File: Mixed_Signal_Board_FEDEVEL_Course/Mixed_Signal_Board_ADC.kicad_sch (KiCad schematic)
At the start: 12 parts, among them U1 REF3033AIDBZT, U300 ADC141S626CIMM_NOPB

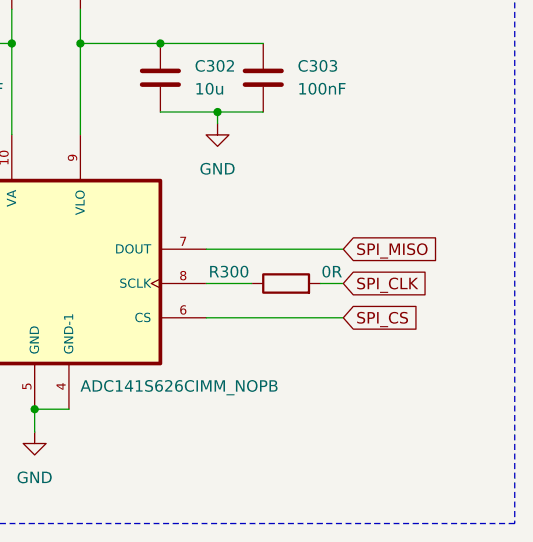
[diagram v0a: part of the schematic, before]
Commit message: Add ADC sch
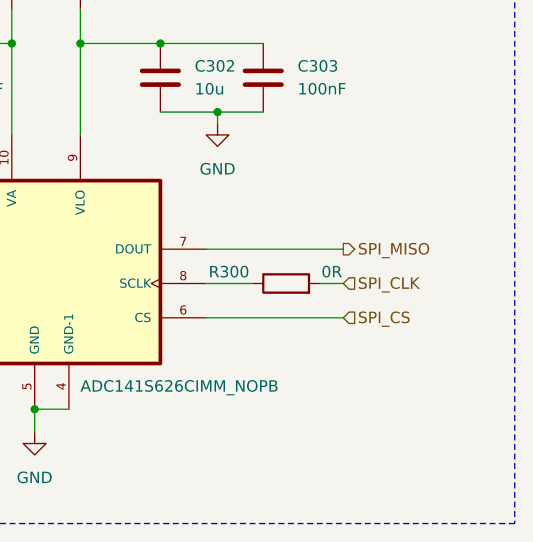
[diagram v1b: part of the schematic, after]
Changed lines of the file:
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@@
 		)
 	)
-	(global_label "SPI_MISO"
+	(hierarchical_label "SPI_CS"
 		(shape input)
-		(at 182.88 69.85 0)
-		(fields_autoplaced yes)
+		(at 182.88 77.47 0)
 		(effects
 			(font
@@
 			(justify left)
 		)
-		(property "Intersheetrefs" "${INTERSHEET_REFS}"
-			(at 194.5133 69.85 0)
-			(hide yes)
-			(show_name no)
-			(do_not_autoplace no)
-			(effects
-				(font
-					(size 1.27 1.27)
-				)
-				(justify left)
-			)
-		)
 	)
-	(global_label "SPI_CLK"
+	(hierarchical_label "SPI_CLK"
 		(shape input)
 		(at 182.88 73.66 0)
-		(fields_autoplaced yes)
 		(effects
 			(font
@@
 			(justify left)
 		)
-		(property "Intersheetrefs" "${INTERSHEET_REFS}"
-			(at 193.4852 73.66 0)
-			(hide yes)
-			(show_name no)
-			(do_not_autoplace no)
-			(effects
-				(font
-					(size 1.27 1.27)
-				)
-				(justify left)
-			)
-		)
 	)
-	(global_label "SPI_CS"
-		(shape input)
-		(at 182.88 77.47 0)
-		(fields_autoplaced yes)
+	(hierarchical_label "SPI_MISO"
+		(shape output)
+		(at 182.88 69.85 0)
 		(effects
 			(font
@@
 			(justify left)
 		)
-		(property "Intersheetrefs" "${INTERSHEET_REFS}"
-			(at 192.3966 77.47 0)
-			(hide yes)
-			(show_name no)
-			(do_not_autoplace no)
-			(effects
-				(font
-					(size 1.27 1.27)
-				)
-				(justify left)
-			)
-		)
 	)

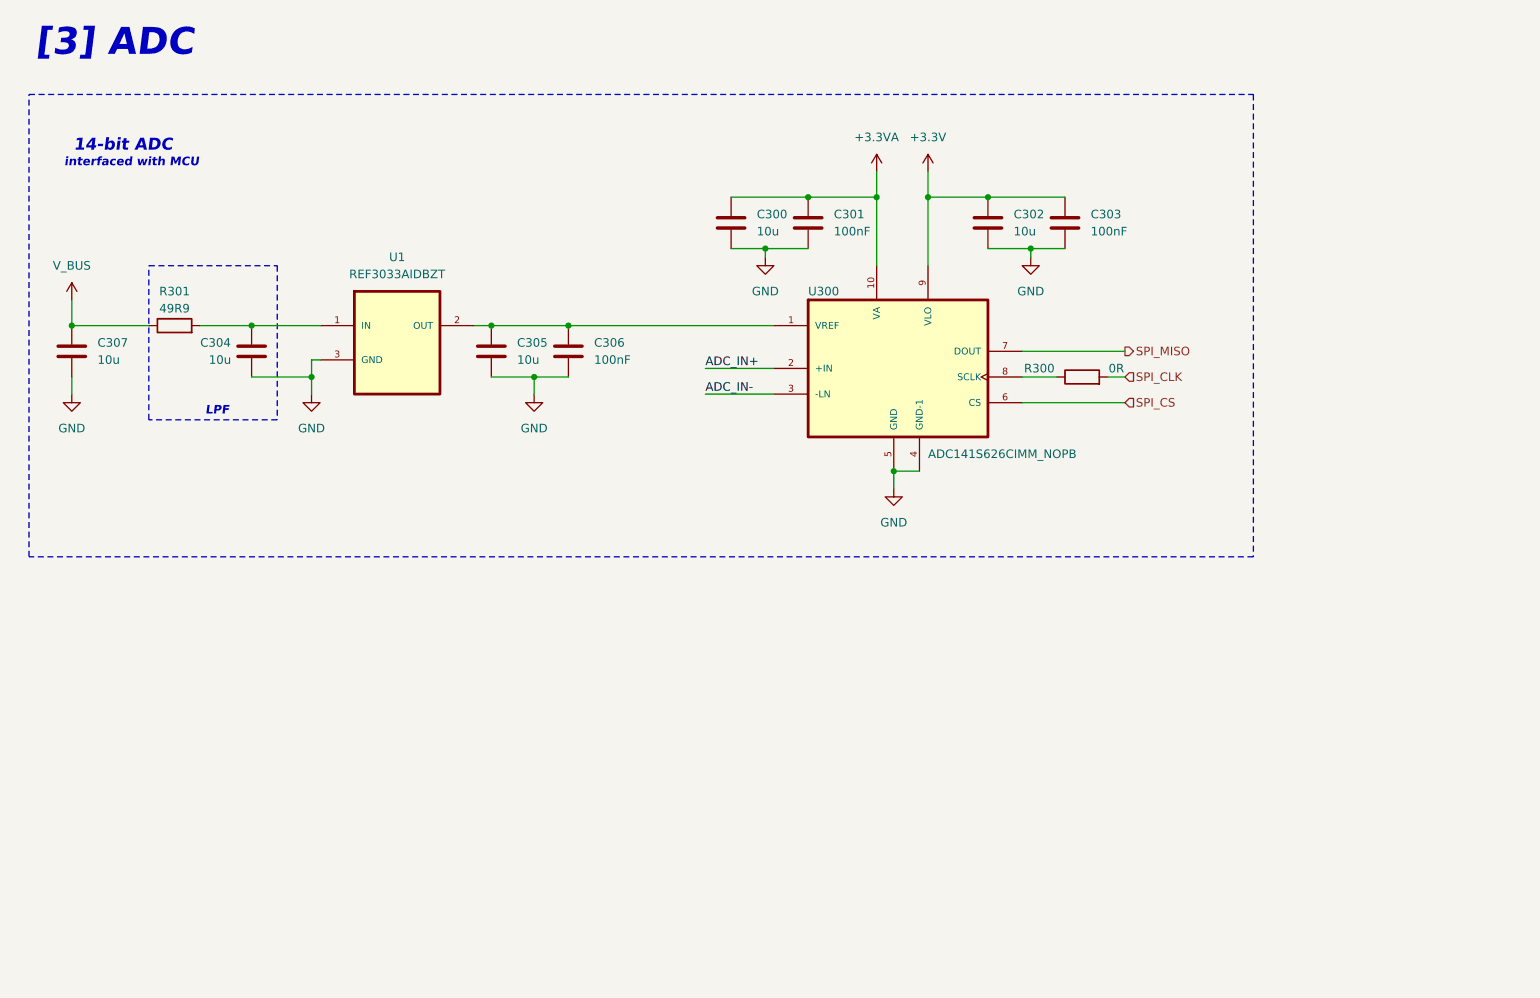
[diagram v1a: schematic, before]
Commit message: Complete the sch of ADC
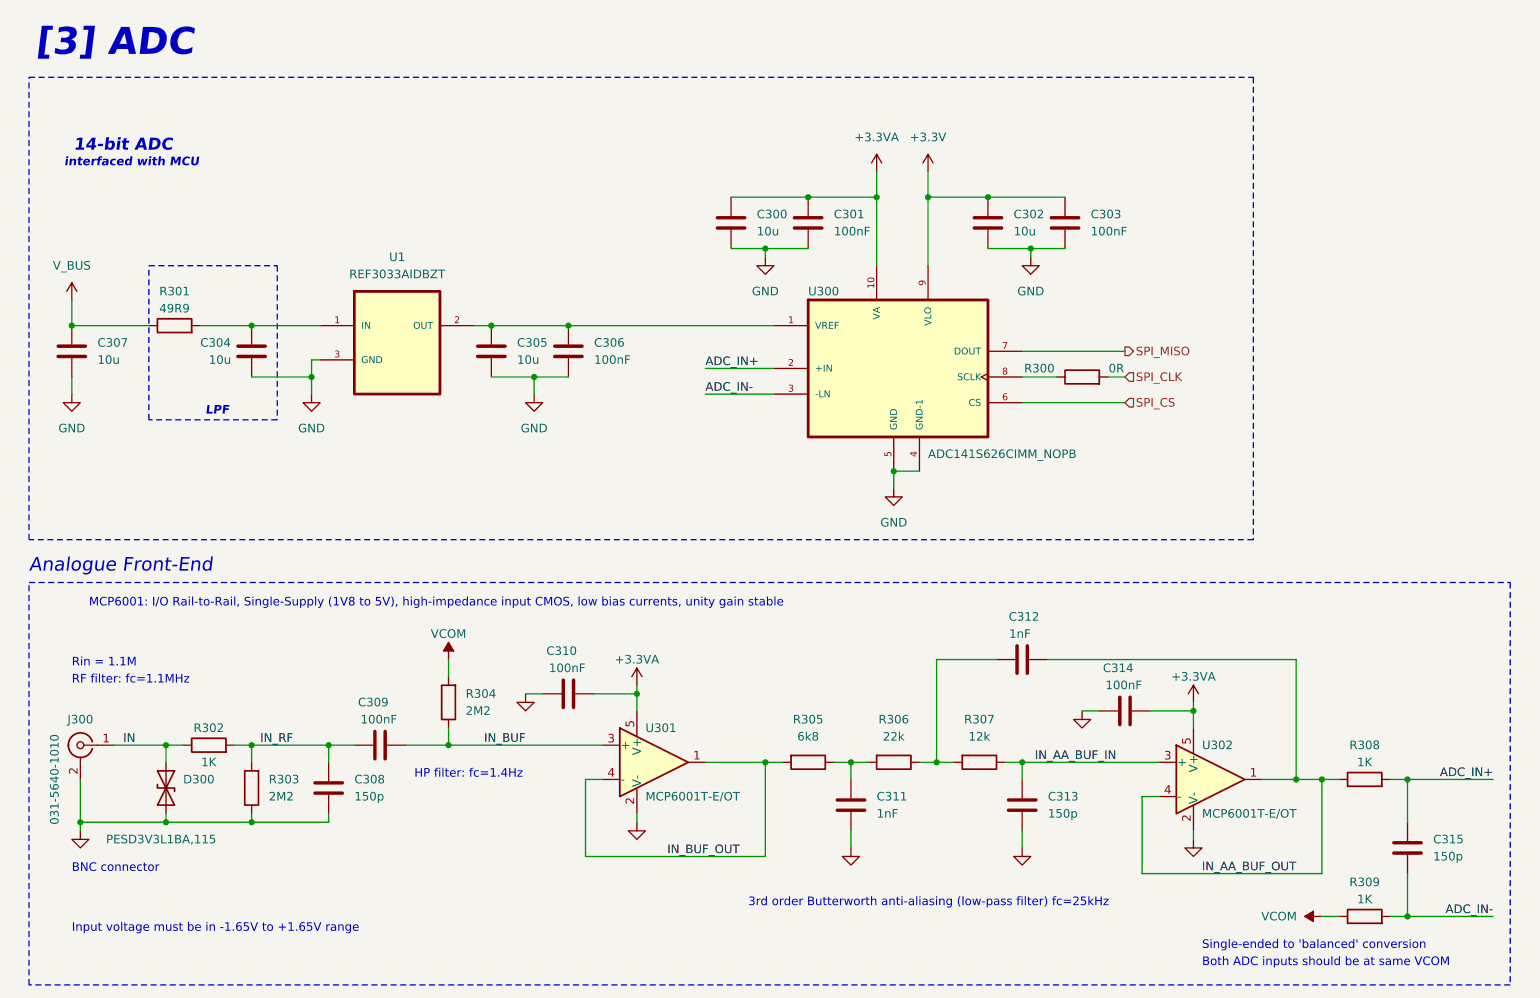
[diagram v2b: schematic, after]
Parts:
- added C308, C313, C315: 150p, Capacitor_SMD:C_0603_1608Metric, symbol Device:C
- added C309, C310, C314: 100nF, Capacitor_SMD:C_0805_2012Metric, symbol Device:C
- added C311, C312: 1nF, Capacitor_SMD:C_0603_1608Metric, symbol Device:C
- added D300: PESD3V3L1BA,115, Diode_SMD:D_SOD-323, symbol Device:D_TVS
- added J300: 031-5640-1010, Connector_Coaxial:BNC_Amphenol_B6252HB-NPP3G-50_Horizontal, symbol Connector:Conn_Coaxial
- added R302, R308, R309: 1K, Resistor_SMD:R_0603_1608Metric, symbol Device:R
- added R303, R304: 2M2, Resistor_SMD:R_0603_1608Metric, symbol Device:R
- added R305: 6k8, Resistor_SMD:R_0603_1608Metric, symbol Device:R
- added R306: 22k, Resistor_SMD:R_0603_1608Metric, symbol Device:R
- added R307: 12k, Resistor_SMD:R_0603_1608Metric, symbol Device:R
- added U301, U302: MCP6001T-E/OT, Package_TO_SOT_SMD:SOT-23-5, symbol Amplifier_Operational:MCP6001-OT
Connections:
- net +3.3VA: now also C310.2, C314.2, U301.5 (V+), U302.5 (V+)
- net ADC_IN+: now also C315.1, R308.2
- net ADC_IN-: now also C315.2, R309.2
- net GND: now also C308.2, C310.1, C311.2, C313.2, C314.1, D300.2 (A2), J300.2 (Ext), R303.1, U301.2 (V-), U302.2 (V-)
- new net: C312.1, R306.1, R307.2
- new net: C311.1, R305.1, R306.2
- new net IN: D300.1 (A1), J300.1 (In), R302.1
- new net IN_AA_BUF_IN: C313.1, R307.1, U302.3 (+)
- new net IN_AA_BUF_OUT: C312.2, R308.1, U302.1, U302.4 (-)
- new net IN_BUF: C309.2, R304.1, U301.3 (+)
- new net IN_BUF_OUT: R305.2, U301.1, U301.4 (-)
- new net IN_RF: C308.1, C309.1, R302.2, R303.2
- new net VCOM: R304.2, R309.1
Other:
- note added: "3rd order Butterworth anti-aliasing (low-pass filter) fc=25kHz"
- note added: "Analogue Front-End"
- note added: "BNC connector"
- note added: "Both ADC inputs should be at same VCOM"
- note added: "HP filter: fc=1.4Hz"
- note added: "Input voltage must be in -1.65V to +1.65V range"
- note added: "MCP6001: I/O Rail-to-Rail, Single-Supply (1V8 to 5V), high-impedance input CMOS, low bias currents, unity gain stable"
- note added: "RF filter: fc=1.1MHz"
- note added: "Rin = 1.1M"
- note added: "Single-ended to 'balanced' conversion"

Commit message: Solve the errors of sch after running the DRC
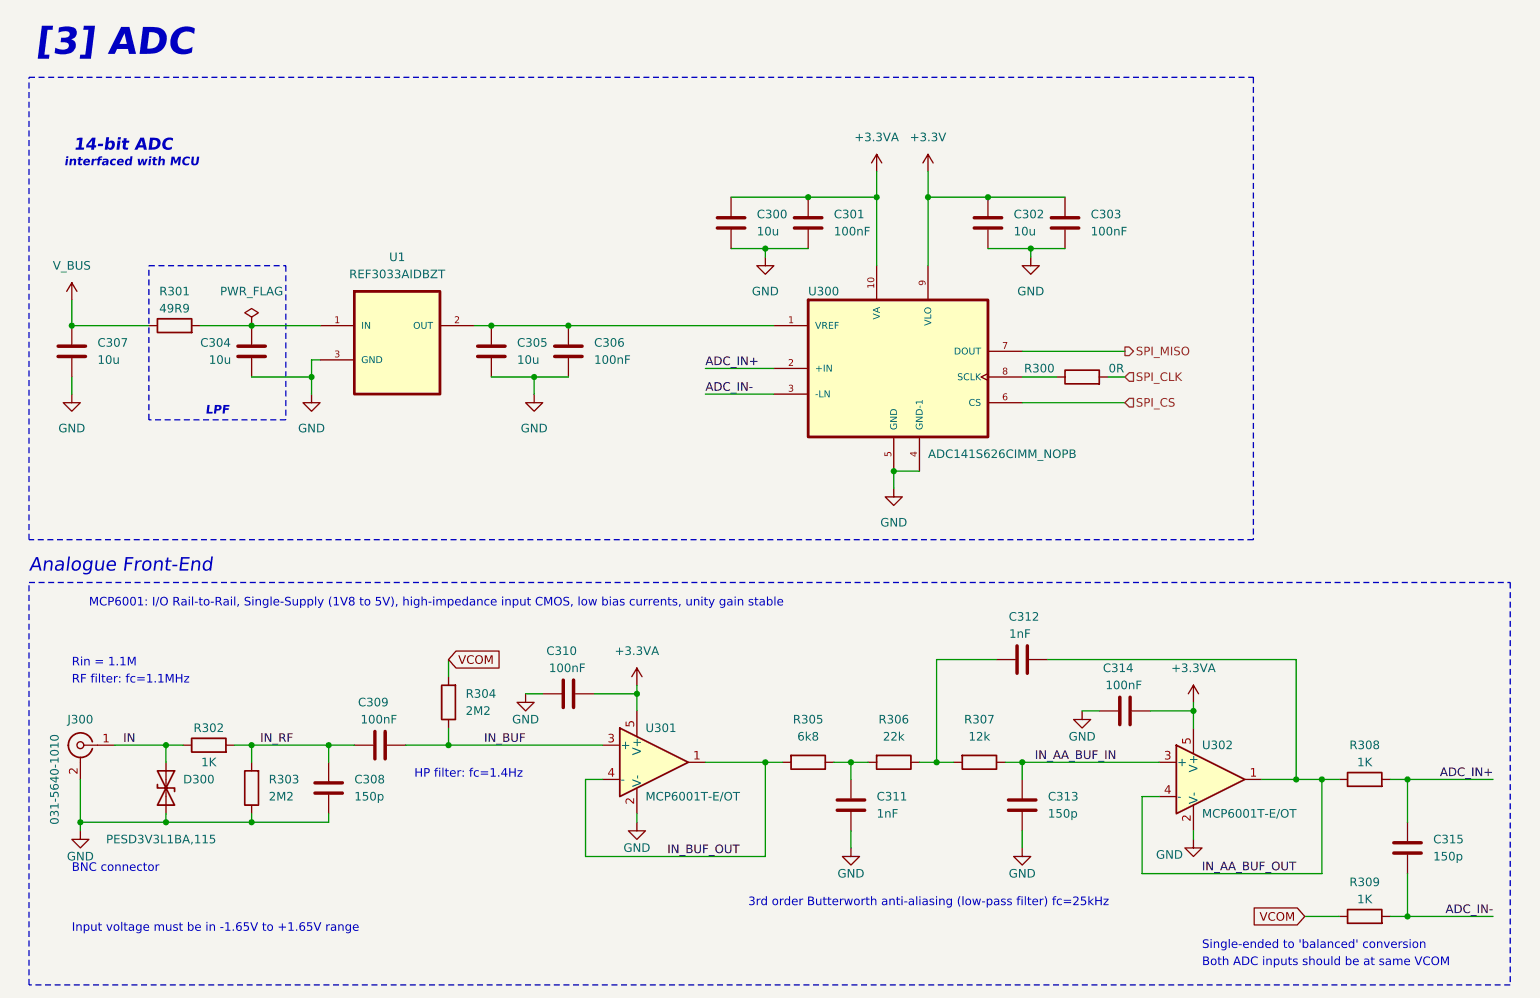
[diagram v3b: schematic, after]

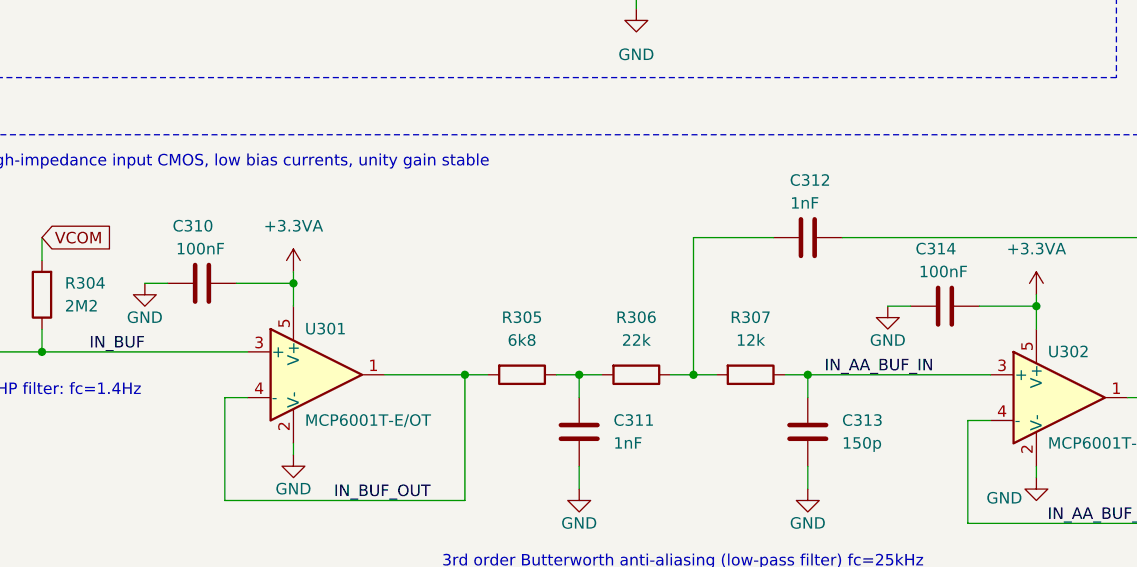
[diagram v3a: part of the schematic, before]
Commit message: Edit the 100nF capacitor to 0603 package
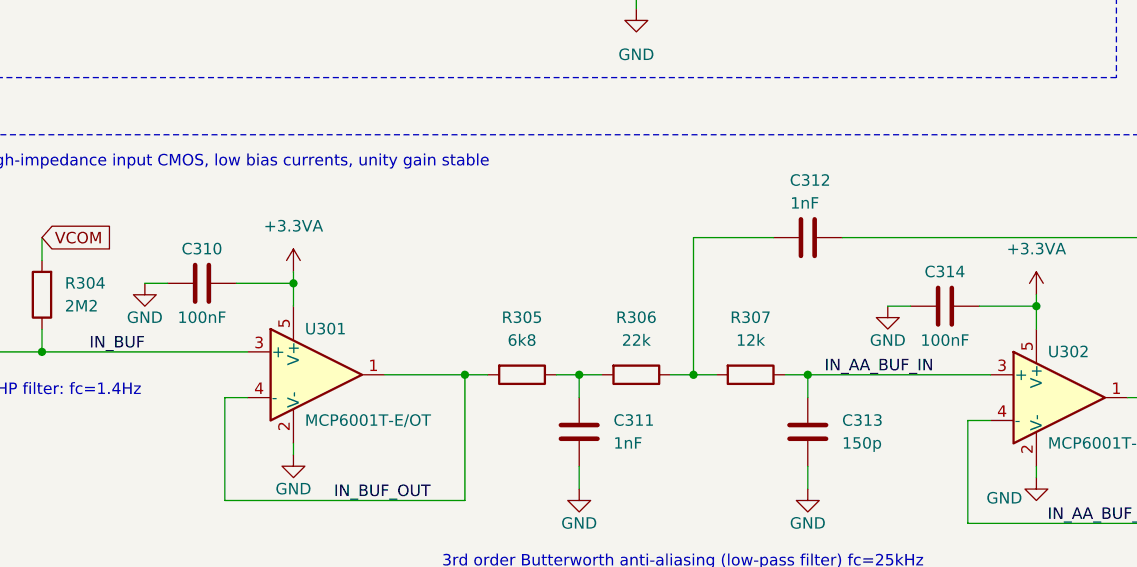
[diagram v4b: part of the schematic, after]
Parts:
- C310, C314: footprint Capacitor_SMD:C_0805_2012Metric -> Capacitor_SMD:C_0603_1608Metric; LCSC_PN C28233 -> C14663; MP CL21B104KCFNNNE -> CC0603KRX7R9BB104

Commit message: Exporting BOM File
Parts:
- U1: Package SOT-23-3 Texas Instruments -> (none)
- U300: Package VSSOP-10 Texas Instruments -> (none)
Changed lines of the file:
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@@
 			)
 		)
-		(property "Package" "SOT-23-3 Texas Instruments"
-			(at 81.28 66.04 0)
-			(hide yes)
-			(show_name no)
-			(do_not_autoplace no)
-			(effects
-				(font
-					(size 1.27 1.27)
-				)
-				(justify bottom)
-			)
-		)
 		(property "OC_FARNELL" "1470325"
 			(at 81.28 66.04 0)
@@
 			(at 148.59 82.55 0)
 			(hide yes)
-			(show_name no)
-			(do_not_autoplace no)
-			(effects
-				(font
-					(size 1.27 1.27)
-				)
-				(justify bottom)
-			)
-		)
-		(property "Package" "VSSOP-10 Texas Instruments"
-			(at 148.59 82.55 0)
-			(hide yes)
